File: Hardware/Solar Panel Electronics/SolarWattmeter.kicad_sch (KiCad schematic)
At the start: 4 parts

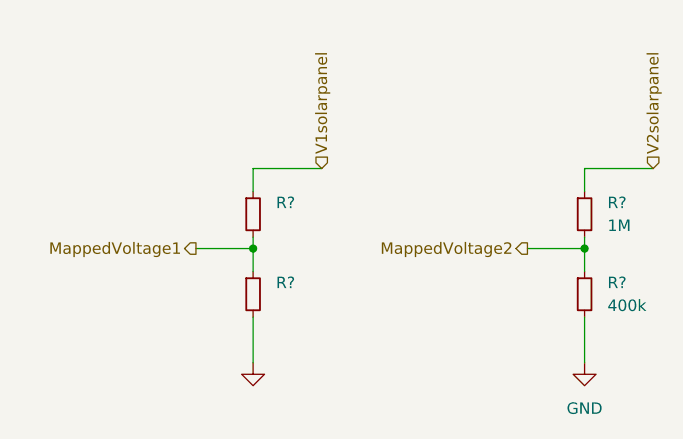
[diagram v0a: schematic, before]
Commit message: Added voltage regulators. Need to size components
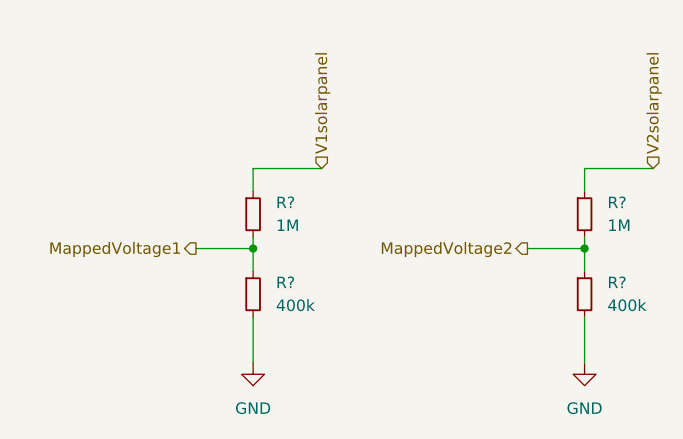
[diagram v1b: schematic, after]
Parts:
- R?: value (none) -> 1M
- R?: value (none) -> 400k
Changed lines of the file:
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@@
       (effects (font (size 1.27 1.27)) hide)
     )
-    (property "Value" "" (id 1) (at 40.64 55.88 0))
+    (property "Value" "GND" (id 1) (at 40.64 55.88 0))
     (property "Footprint" "" (id 2) (at 40.64 50.8 0)
       (effects (font (size 1.27 1.27)) hide)
@@
       (effects (font (size 1.27 1.27)) (justify left))
     )
-    (property "Value" "" (id 1) (at 43.18 35.5599 0)
+    (property "Value" "1M" (id 1) (at 43.18 35.5599 0)
       (effects (font (size 1.27 1.27)) (justify left))
     )
@@
       (effects (font (size 1.27 1.27)) (justify left))
     )
-    (property "Value" "" (id 1) (at 43.18 44.4499 0)
+    (property "Value" "400k" (id 1) (at 43.18 44.4499 0)
       (effects (font (size 1.27 1.27)) (justify left))
     )
